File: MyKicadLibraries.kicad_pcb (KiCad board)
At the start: 2 copper layers, 184.4 x 134.7 mm, 42 parts, among them J1 Conn_01x08, J10 RCJ-22, J11 DIN-5, J12 Mini-DIN-6, J13 USB_A, J14 Conn_01x02, J15 Conn_01x02, J2 Conn_01x08, J3 POGO Pins, J4 c8-inlet, J5 FTDI, J6 Micro_SD_Card, J7 Conn_01x04, J8 Conn_02x04_Counter_Clockwise, J9 Conn_01x04, SW1 Schurter Switch, SW2 POWER, U1 radio-receiver, U10 rdm-6300, U11 magnetic-charger, U12 adafruit-MAX98357, U13 TTL, U14 lxb18, U15 esp32-wemos-d1-mini, U16 TCRT5000, U17 opb607a, U18 max98367, U19 esp-01f, U2 tp4056, U20 m18, U21 bme280, U23 mems-mic, U3 LilygoSIMT7000G, U4 esp-01m, U5 relais_module, U6 ESP-01, U7 dcdc, U8 mems-mic, U9 ESP-12E

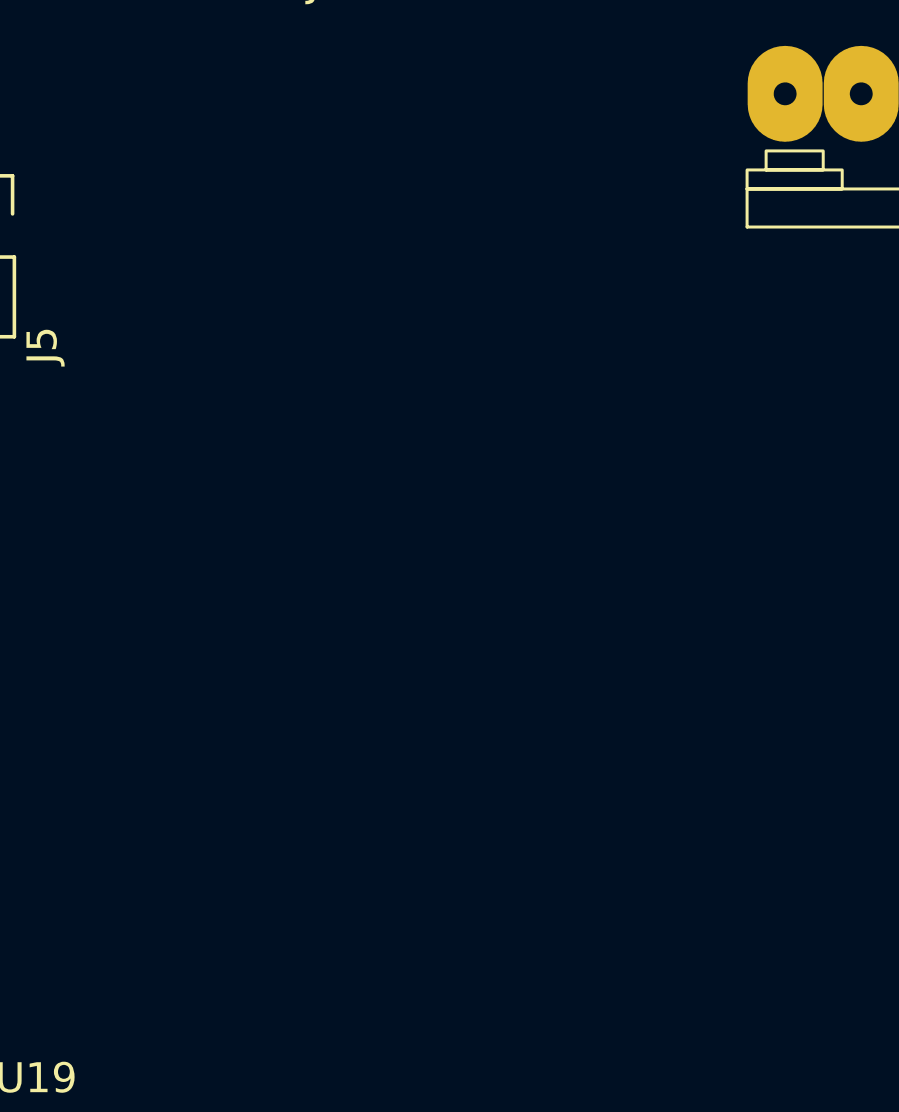
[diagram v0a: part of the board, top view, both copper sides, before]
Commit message: Add lipo charger module
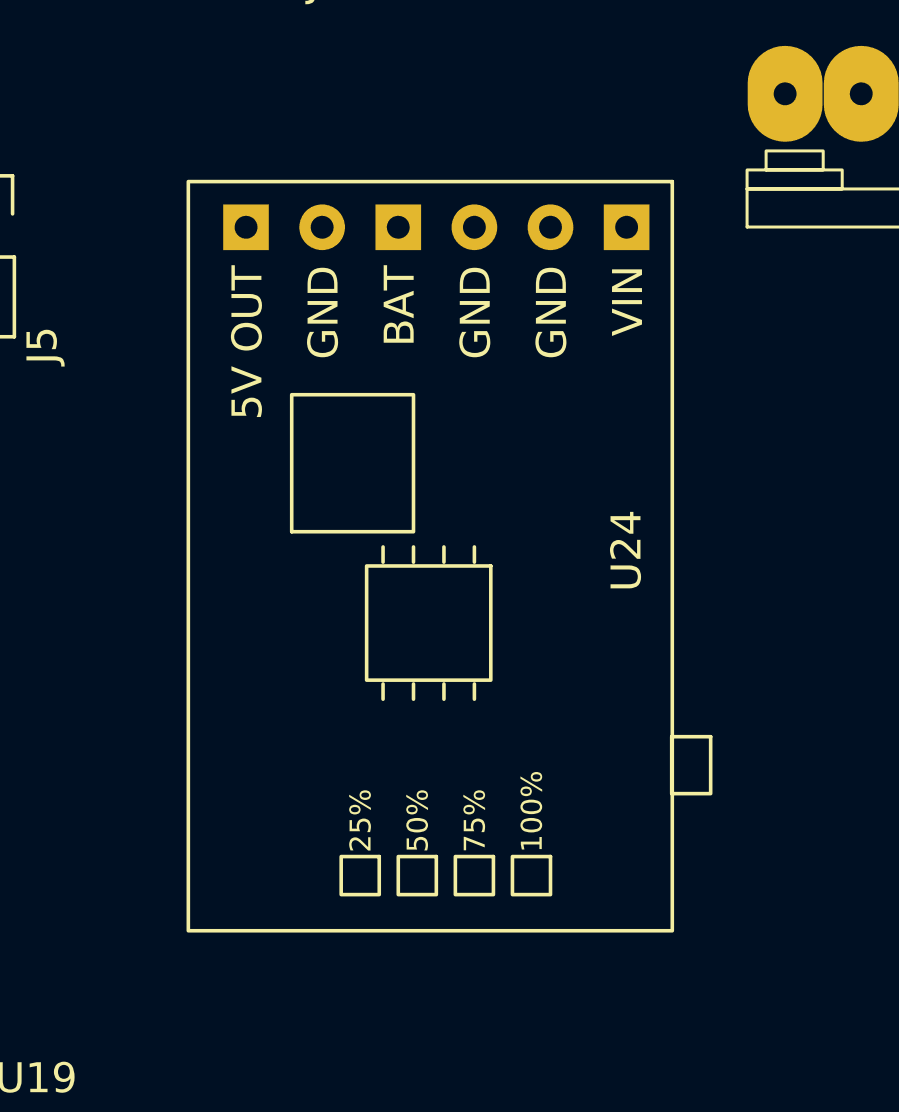
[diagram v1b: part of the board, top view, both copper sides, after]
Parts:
- added U24: ~, charge-module:charge-module, F.Cu at (119.5, 102.6)
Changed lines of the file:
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@@
   (net 299 "unconnected-(SW2-B-Pad2)")
   (net 300 "unconnected-(SW2-C-Pad3)")
+  (net 301 "unconnected-(U24-VIN-Pad1)")
+  (net 302 "unconnected-(U24-GND-Pad2)")
+  (net 303 "unconnected-(U24-GND-Pad3)")
+  (net 304 "unconnected-(U24-BAT+-Pad4)")
+  (net 305 "unconnected-(U24-GND-Pad5)")
+  (net 306 "unconnected-(U24-VOUT-Pad6)")
   (footprint "esp-01f:esp-01f" (layer "F.Cu")
     (at 114.405 137.985)
@@
     )
   )
+  (footprint "charge-module:charge-module" (layer "F.Cu")
+    (at 119.5 102.6 90)
+    (property "Sheetfile" "MyKicadLibraries.kicad_sch")
+    (property "Sheetname" "")
+    (attr through_hole)
+    (fp_text reference "U24" (at -10.795 12.7 90 unlocked) (layer "F.SilkS")
+        (effects (font (size 1 1) (thickness 0.15)))
+    )
+    (fp_text value "~" (at -12.065 0 90 unlocked) (layer "F.Fab")
+        (effects (font (size 1 1) (thickness 0.15)))
+    )
+    (fp_text user "75%" (at -20.869849 8.049854 90 unlocked) (layer "F.SilkS")
+        (effects (font (size 0.7 0.7) (thickness 0.15)) (justify left bottom))
+    )
+    (fp_text user "BAT" (at -1.27 5.715 90 unlocked) (layer "F.SilkS")
+        (effects (font (size 1 1) (thickness 0.15)) (justify right bottom))
+    )
+    (fp_text user "GND" (at -1.27 8.255 90 unlocked) (layer "F.SilkS")
+        (effects (font (size 1 1) (thickness 0.15)) (justify right bottom))
+    )
+    (fp_text user "GND" (at -1.27 3.175 90 unlocked) (layer "F.SilkS")
+        (effects (font (size 1 1) (thickness 0.15)) (justify right bottom))
+    )
+    (fp_text user "5V OUT" (at -1.27 0.635 90 unlocked) (layer "F.SilkS")
+        (effects (font (size 1 1) (thickness 0.15)) (justify right bottom))
+    )
+    (fp_text user "100%" (at -20.869849 9.954854 90 unlocked) (layer "F.SilkS")
+        (effects (font (size 0.7 0.7) (thickness 0.15)) (justify left bottom))
+    )
+    (fp_text user "GND" (at -1.27 10.795 90 unlocked) (layer "F.SilkS")
+        (effects (font (size 1 1) (thickness 0.15)) (justify right bottom))
+    )
+    (fp_text user "50%" (at -20.869849 6.144854 90 unlocked) (layer "F.SilkS")
+        (effects (font (size 0.7 0.7) (thickness 0.15)) (justify left bottom))
+    )
+    (fp_text user "VIN" (at -1.27 13.335 90 unlocked) (layer "F.SilkS")
+        (effects (font (size 1 1) (thickness 0.15)) (justify right bottom))
+    )
+    (fp_text user "25%" (at -20.869849 4.239854 90 unlocked) (layer "F.SilkS")
+        (effects (font (size 0.7 0.7) (thickness 0.15)) (justify left bottom))
+    )
+    (fp_text user "${REFERENCE}" (at -7.62 -2.54 90 unlocked) (layer "F.Fab")
+        (effects (font (size 1 1) (thickness 0.15)))
+    )
+    (fp_line (start -15.748 4.572) (end -15.24 4.572)
+      (stroke (width 0.12) (type default)) (layer "F.SilkS"))
+    (fp_line (start -15.748 5.588) (end -15.24 5.588)
+      (stroke (width 0.12) (type default)) (layer "F.SilkS"))
+    (fp_line (start -15.748 6.604) (end -15.24 6.604)
+      (stroke (width 0.12) (type default)) (layer "F.SilkS"))
+    (fp_line (start -15.748 7.62) (end -15.24 7.62)
+      (stroke (width 0.12) (type default)) (layer "F.SilkS"))
+    (fp_line (start -11.176 4.572) (end -10.668 4.572)
+      (stroke (width 0.12) (type default)) (layer "F.SilkS"))
+    (fp_line (start -11.176 5.588) (end -10.668 5.588)
+      (stroke (width 0.12) (type default)) (layer "F.SilkS"))
+    (fp_line (start -11.176 6.604) (end -10.668 6.604)
+      (stroke (width 0.12) (type default)) (layer "F.SilkS"))
+    (fp_line (start -11.176 7.62) (end -10.668 7.62)
+      (stroke (width 0.12) (type default)) (layer "F.SilkS"))
+    (fp_rect (start -21 4.445) (end -22.27 3.175)
+      (stroke (width 0.12) (type default)) (fill none) (layer "F.SilkS"))
+    (fp_rect (start -21 6.35) (end -22.27 5.08)
+      (stroke (width 0.12) (type default)) (fill none) (layer "F.SilkS"))
+    (fp_rect (start -21 8.255) (end -22.27 6.985)
+      (stroke (width 0.12) (type default)) (fill none) (layer "F.SilkS"))
+    (fp_rect (start -21 10.16) (end -22.27 8.89)
+      (stroke (width 0.12) (type default)) (fill none) (layer "F.SilkS"))
+    (fp_rect (start -17 15.504644) (end -18.9 14.204644)
+      (stroke (width 0.12) (type default)) (fill none) (layer "F.SilkS"))
+    (fp_rect (start -11.303 8.168) (end -15.113 4.024)
+      (stroke (width 0.12) (type default)) (fill none) (layer "F.SilkS"))
+    (fp_rect (start -10.16 1.524) (end -5.588 5.588)
+      (stroke (width 0.12) (type default)) (fill none) (layer "F.SilkS"))
+    (fp_rect (start 1.524 14.224) (end -23.476 -1.926)
+      (stroke (width 0.12) (type default)) (fill none) (layer "F.SilkS"))
+    (pad "1" thru_hole rect (at 0 12.7 90) (size 1.524 1.524) (drill 0.762) (layers "*.Cu" "*.Mask")
+      (net 301 "unconnected-(U24-VIN-Pad1)") (pinfunction "VIN") (pintype "power_in"))
+    (pad "2" thru_hole circle (at 0 10.16 90) (size 1.524 1.524) (drill 0.762) (layers "*.Cu" "*.Mask")
+      (net 302 "unconnected-(U24-GND-Pad2)") (pinfunction "GND") (pintype "power_in"))
+    (pad "3" thru_hole circle (at 0 7.62 90) (size 1.524 1.524) (drill 0.762) (layers "*.Cu" "*.Mask")
+      (net 303 "unconnected-(U24-GND-Pad3)") (pinfunction "GND") (pintype "power_in"))
+    (pad "4" thru_hole rect (at 0 5.08 90) (size 1.524 1.524) (drill 0.762) (layers "*.Cu" "*.Mask")
+      (net 304 "unconnected-(U24-BAT+-Pad4)") (pinfunction "BAT+") (pintype "power_in"))
+    (pad "5" thru_hole circle (at 0 2.54 90) (size 1.524 1.524) (drill 0.762) (layers "*.Cu" "*.Mask")
+      (net 305 "unconnected-(U24-GND-Pad5)") (pinfunction "GND") (pintype "power_in"))
+    (pad "6" thru_hole rect (at 0 0 90) (size 1.524 1.524) (drill 0.762) (layers "*.Cu" "*.Mask")
+      (net 306 "unconnected-(U24-VOUT-Pad6)") (pinfunction "VOUT") (pintype "power_in"))
+  )
   (footprint "mems-mic:mems-mic-round" (layer "F.Cu")

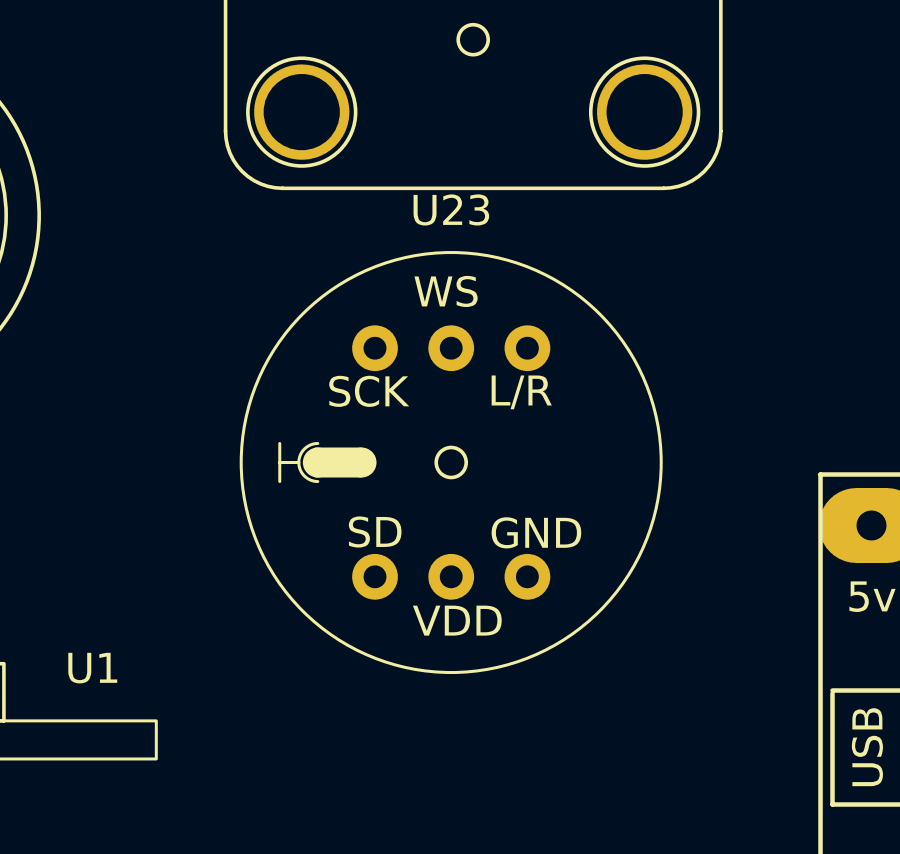
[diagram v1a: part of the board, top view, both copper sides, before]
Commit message: Fix mems-mic pin assignment
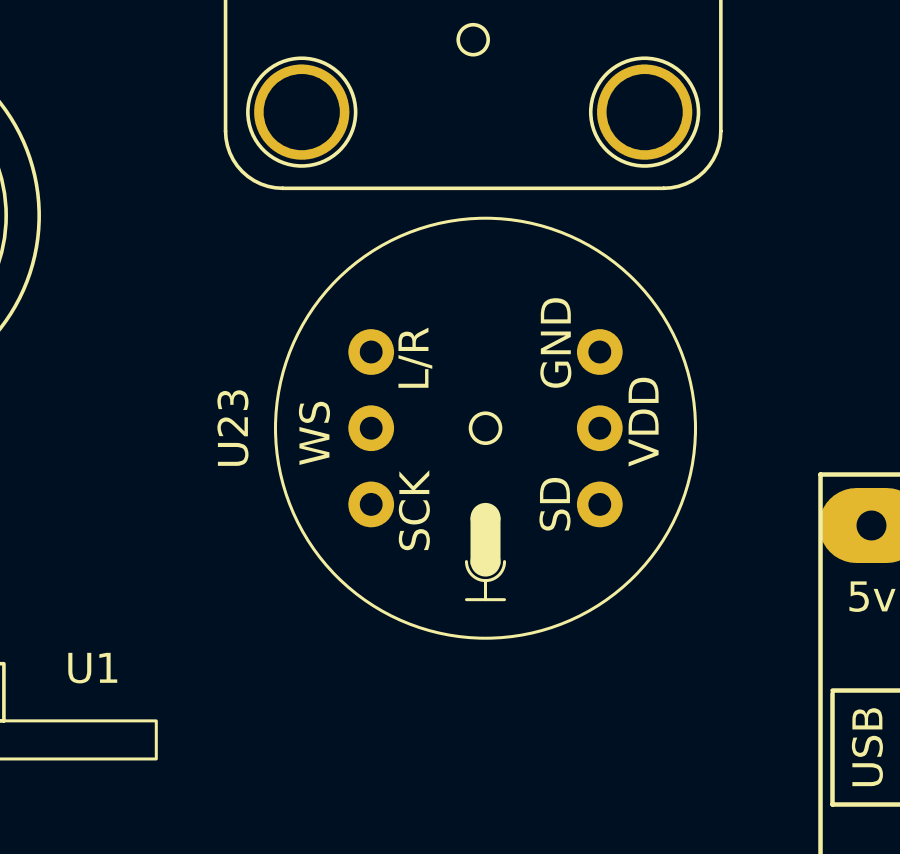
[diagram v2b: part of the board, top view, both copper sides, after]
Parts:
- moved U23 1.62 mm to (175.1, 91.6), turned to 90 degrees
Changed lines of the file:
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@@
+    )
+  )
+  (footprint "mems-mic:mems-mic-round" (layer "F.Cu")
+    (at 175.133 91.567 90)
+    (property "Sheetfile" "MyKicadLibraries.kicad_sch")
+    (property "Sheetname" "")
+    (attr through_hole)
+    (fp_text reference "U23" (at 0 -8.382 90) (layer "F.SilkS")
+        (effects (font (size 1 1) (thickness 0.15)))
+    )
+    (fp_text value "mems-mic" (at 0 -10.922 90) (layer "F.Fab")
+        (effects (font (size 1 1) (thickness 0.15)))
+    )
+    (fp_text user "WS" (at -1.27 -5.08 90 unlocked) (layer "F.SilkS")
+        (effects (font (size 1 1) (thickness 0.1)) (justify left bottom))
+    )
+    (fp_text user "SCK" (at -4.156642 -1.750172 90 unlocked) (layer "F.SilkS")
+        (effects (font (size 1 1) (thickness 0.1)) (justify left bottom))
+    )
+    (fp_text user "VDD" (at -1.287056 5.892585 90 unlocked) (layer "F.SilkS")
+        (effects (font (size 1 1) (thickness 0.1)) (justify left bottom))
+    )
+    (fp_text user "SD" (at -3.503172 2.937764 90 unlocked) (layer "F.SilkS")
+        (effects (font (size 1 1) (thickness 0.1)) (justify left bottom))
+    )
+    (fp_text user "GND" (at 1.269999 2.966176 90 unlocked) (layer "F.SilkS")
+        (effects (font (size 1 1) (thickness 0.1)) (justify left bottom))
+    )
+    (fp_text user "L/R" (at 1.213176 -1.778584 90 unlocked) (layer "F.SilkS")
+        (effects (font (size 1 1) (thickness 0.1)) (justify left bottom))
+    )
+    (fp_line (start -5.715 -0.635) (end -5.715 0.635)
+      (stroke (width 0.1) (type default)) (layer "F.SilkS"))
+    (fp_line (start -5.715 0) (end -5.08 0)
+      (stroke (width 0.1) (type default)) (layer "F.SilkS"))
+    (fp_rect (start -4.525 -0.45) (end -2.99 0.45)
+      (stroke (width 0.1) (type solid)) (fill solid) (layer "F.SilkS"))
+    (fp_arc (start -4.445 0.635) (mid -5.08 0) (end -4.445 -0.635)
+      (stroke (width 0.1) (type default)) (layer "F.SilkS"))
+    (fp_circle (center -4.445 0) (end -3.995 0)
+      (stroke (width 0.1) (type solid)) (fill solid) (layer "F.SilkS"))
+    (fp_circle (center -2.99 0) (end -2.54 0)
+      (stroke (width 0.1) (type solid)) (fill solid) (layer "F.SilkS"))
+    (fp_circle (center 0 0) (end 0.5 0)
+      (stroke (width 0.12) (type solid)) (fill none) (layer "F.SilkS"))
+    (fp_circle (center 0 0) (end 7 0)
+      (stroke (width 0.1) (type default)) (fill none) (layer "F.SilkS"))
+    (pad "1" thru_hole circle (at 0 3.81 90) (size 1.524 1.524) (drill 0.762) (layers "*.Cu" "*.Mask")
+      (net 292 "unconnected-(U23-3V-Pad1)") (pinfunction "3V") (pintype "power_in"))
+    (pad "2" thru_hole circle (at 2.54 3.81 90) (size 1.524 1.524) (drill 0.762) (layers "*.Cu" "*.Mask")
+      (net 293 "unconnected-(U23-GND-Pad2)") (pinfunction "GND") (pintype "power_in"))
+    (pad "3" thru_hole circle (at -2.54 -3.81 90) (size 1.524 1.524) (drill 0.762) (layers "*.Cu" "*.Mask")
+      (net 294 "unconnected-(U23-BCLK-Pad3)") (pinfunction "BCLK") (pintype "input"))
+    (pad "4" thru_hole circle (at -2.54 3.81 90) (size 1.524 1.524) (drill 0.762) (layers "*.Cu" "*.Mask")
+      (net 295 "unconnected-(U23-DOUT-Pad4)") (pinfunction "DOUT") (pintype "output"))
+    (pad "5" thru_hole circle (at 0 -3.81 90) (size 1.524 1.524) (drill 0.762) (layers "*.Cu" "*.Mask")
+      (net 296 "unconnected-(U23-LRCLK-Pad5)") (pinfunction "LRCLK") (pintype "input"))
+    (pad "6" thru_hole circle (at 2.54 -3.81 90) (size 1.524 1.524) (drill 0.762) (layers "*.Cu" "*.Mask")
+      (net 297 "unconnected-(U23-SEL-Pad6)") (pinfunction "SEL") (pintype "input"))
+    (model "${KIPRJMOD}/lib/mems-mic/mems-mic-round.step"
+      (offset (xyz 0 0 3.2))
+      (scale (xyz 1 1 1))
+      (rotate (xyz 90 0 0))
+    )
+    (model ":KICAD7_3DMODEL_DIR:Connector_PinHeader_2.54mm.3dshapes/PinHeader_1x03_P2.54mm_Vertical.step"
+      (offset (xyz 2.54 3.81 0))
+      (scale (xyz 1 1 1))
+      (rotate (xyz 0 0 90))
+    )
+    (model ":KICAD7_3DMODEL_DIR:Connector_PinHeader_2.54mm.3dshapes/PinHeader_1x03_P2.54mm_Vertical.step"
+      (offset (xyz 2.54 -3.81 0))
+      (scale (xyz 1 1 1))
+      (rotate (xyz 0 0 90))
     )
   )
@@
       (net 306 "unconnected-(U24-VOUT-Pad6)") (pinfunction "VOUT") (pintype "power_in"))
   )
-  (footprint "mems-mic:mems-mic-round" (layer "F.Cu")
-    (at 173.99 92.71)
-    (property "Sheetfile" "MyKicadLibraries.kicad_sch")
-    (property "Sheetname" "")
-    (attr through_hole)
-    (fp_text reference "U23" (at 0 -8.382) (layer "F.SilkS")
-        (effects (font (size 1 1) (thickness 0.15)))
-    )
-    (fp_text value "mems-mic" (at 0 -10.922) (layer "F.Fab")
-        (effects (font (size 1 1) (thickness 0.15)))
-    )
-    (fp_text user "L/R" (at 1.213176 -1.778584 unlocked) (layer "F.SilkS")
-        (effects (font (size 1 1) (thickness 0.1)) (justify left bottom))
-    )
-    (fp_text user "SD" (at -3.503172 2.937764 unlocked) (layer "F.SilkS")
-        (effects (font (size 1 1) (thickness 0.1)) (justify left bottom))
-    )
-    (fp_text user "GND" (at 1.269999 2.966176 unlocked) (layer "F.SilkS")
-        (effects (font (size 1 1) (thickness 0.1)) (justify left bottom))
-    )
-    (fp_text user "WS" (at -1.27 -5.08 unlocked) (layer "F.SilkS")
-        (effects (font (size 1 1) (thickness 0.1)) (justify left bottom))
-    )
-    (fp_text user "VDD" (at -1.287056 5.892585 unlocked) (layer "F.SilkS")
-        (effects (font (size 1 1) (thickness 0.1)) (justify left bottom))
-    )
-    (fp_text user "SCK" (at -4.156642 -1.750172 unlocked) (layer "F.SilkS")
-        (effects (font (size 1 1) (thickness 0.1)) (justify left bottom))
-    )
-    (fp_line (start -5.715 -0.635) (end -5.715 0.635)
-      (stroke (width 0.1) (type default)) (layer "F.SilkS"))
-    (fp_line (start -5.715 0) (end -5.08 0)
-      (stroke (width 0.1) (type default)) (layer "F.SilkS"))
-    (fp_rect (start -4.525 -0.45) (end -2.99 0.45)
-      (stroke (width 0.1) (type solid)) (fill solid) (layer "F.SilkS"))
-    (fp_arc (start -4.445 0.635) (mid -5.08 0) (end -4.445 -0.635)
-      (stroke (width 0.1) (type default)) (layer "F.SilkS"))
-    (fp_circle (center -4.445 0) (end -3.995 0)
-      (stroke (width 0.1) (type solid)) (fill solid) (layer "F.SilkS"))
-    (fp_circle (center -2.99 0) (end -2.54 0)
-      (stroke (width 0.1) (type solid)) (fill solid) (layer "F.SilkS"))
-    (fp_circle (center 0 0) (end 0.5 0)
-      (stroke (width 0.12) (type solid)) (fill none) (layer "F.SilkS"))
-    (fp_circle (center 0 0) (end 7 0)
-      (stroke (width 0.1) (type default)) (fill none) (layer "F.SilkS"))
-    (pad "1" thru_hole circle (at 0 3.81) (size 1.524 1.524) (drill 0.762) (layers "*.Cu" "*.Mask")
-      (net 292 "unconnected-(U23-3V-Pad1)") (pinfunction "3V") (pintype "power_in"))
-    (pad "2" thru_hole circle (at 2.54 3.81) (size 1.524 1.524) (drill 0.762) (layers "*.Cu" "*.Mask")
-      (net 293 "unconnected-(U23-GND-Pad2)") (pinfunction "GND") (pintype "power_in"))
-    (pad "3" thru_hole circle (at -2.54 -3.81) (size 1.524 1.524) (drill 0.762) (layers "*.Cu" "*.Mask")
-      (net 294 "unconnected-(U23-BCLK-Pad3)") (pinfunction "BCLK") (pintype "input"))
-    (pad "4" thru_hole circle (at -2.54 3.81) (size 1.524 1.524) (drill 0.762) (layers "*.Cu" "*.Mask")
-      (net 295 "unconnected-(U23-DOUT-Pad4)") (pinfunction "DOUT") (pintype "output"))
-    (pad "5" thru_hole circle (at 2.54 -3.81) (size 1.524 1.524) (drill 0.762) (layers "*.Cu" "*.Mask")
-      (net 296 "unconnected-(U23-LRCLK-Pad5)") (pinfunction "LRCLK") (pintype "input"))
-    (pad "6" thru_hole circle (at 0 -3.81) (size 1.524 1.524) (drill 0.762) (layers "*.Cu" "*.Mask")
-      (net 297 "unconnected-(U23-SEL-Pad6)") (pinfunction "SEL") (pintype "input"))
-    (model "${KIPRJMOD}/lib/mems-mic/mems-mic-round.step"
-      (offset (xyz 0 0 3.2))
-      (scale (xyz 1 1 1))
-      (rotate (xyz 90 0 0))
-    )
-    (model ":KICAD7_3DMODEL_DIR:Connector_PinHeader_2.54mm.3dshapes/PinHeader_1x03_P2.54mm_Vertical.step"
-      (offset (xyz 2.54 3.81 0))
-      (scale (xyz 1 1 1))
-      (rotate (xyz 0 0 90))
-    )
-    (model ":KICAD7_3DMODEL_DIR:Connector_PinHeader_2.54mm.3dshapes/PinHeader_1x03_P2.54mm_Vertical.step"
-      (offset (xyz 2.54 -3.81 0))
-      (scale (xyz 1 1 1))
-      (rotate (xyz 0 0 90))
-    )
-  )
   (footprint "radio-receiver:radio-receiver" (layer "F.Cu")
